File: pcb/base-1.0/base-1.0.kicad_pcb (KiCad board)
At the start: 2 copper layers, 85.6 x 54 mm, 0 parts

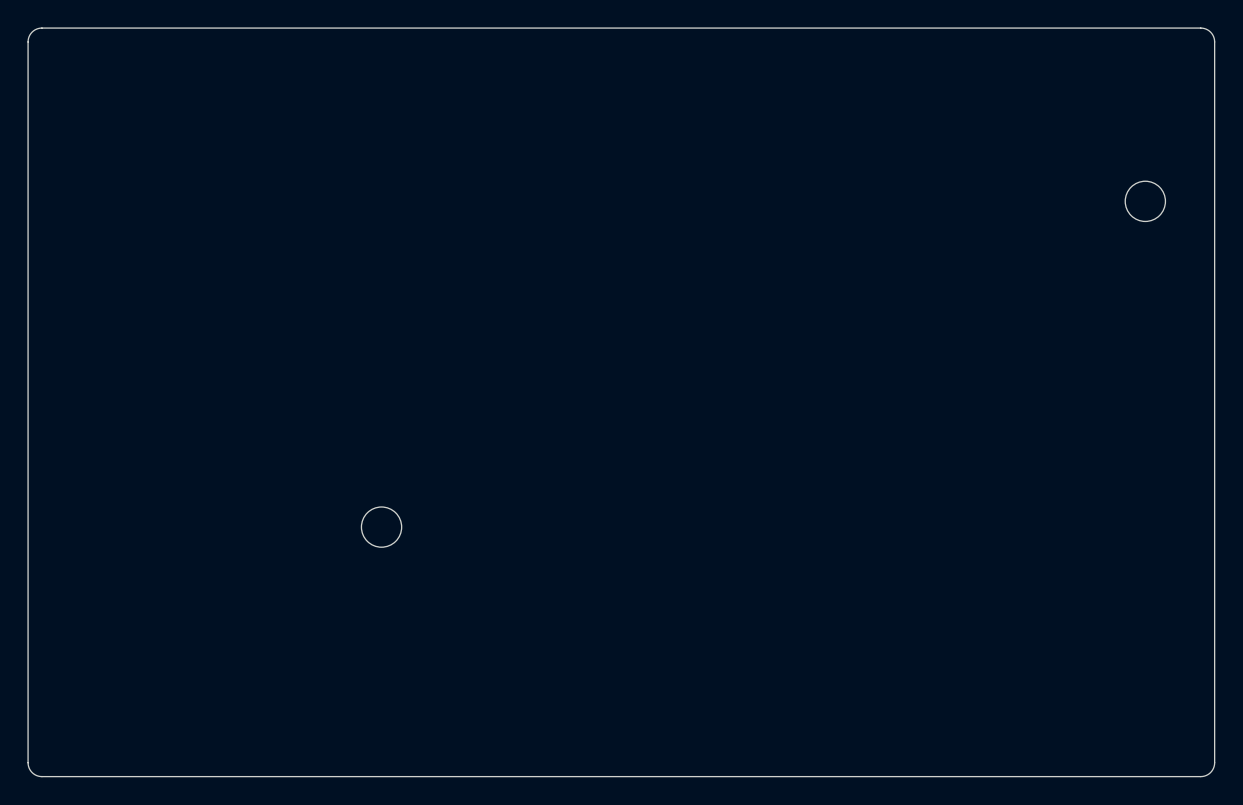
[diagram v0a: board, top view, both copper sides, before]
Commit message: o Adding IO extender for RPI header. o Adding mounting holes in schematic and PCB. o Fixing bad footprint: Capacitor_SMD:CP_Elec_8x10.2 => Capacitor_SMD:CP_Elec_8x10.
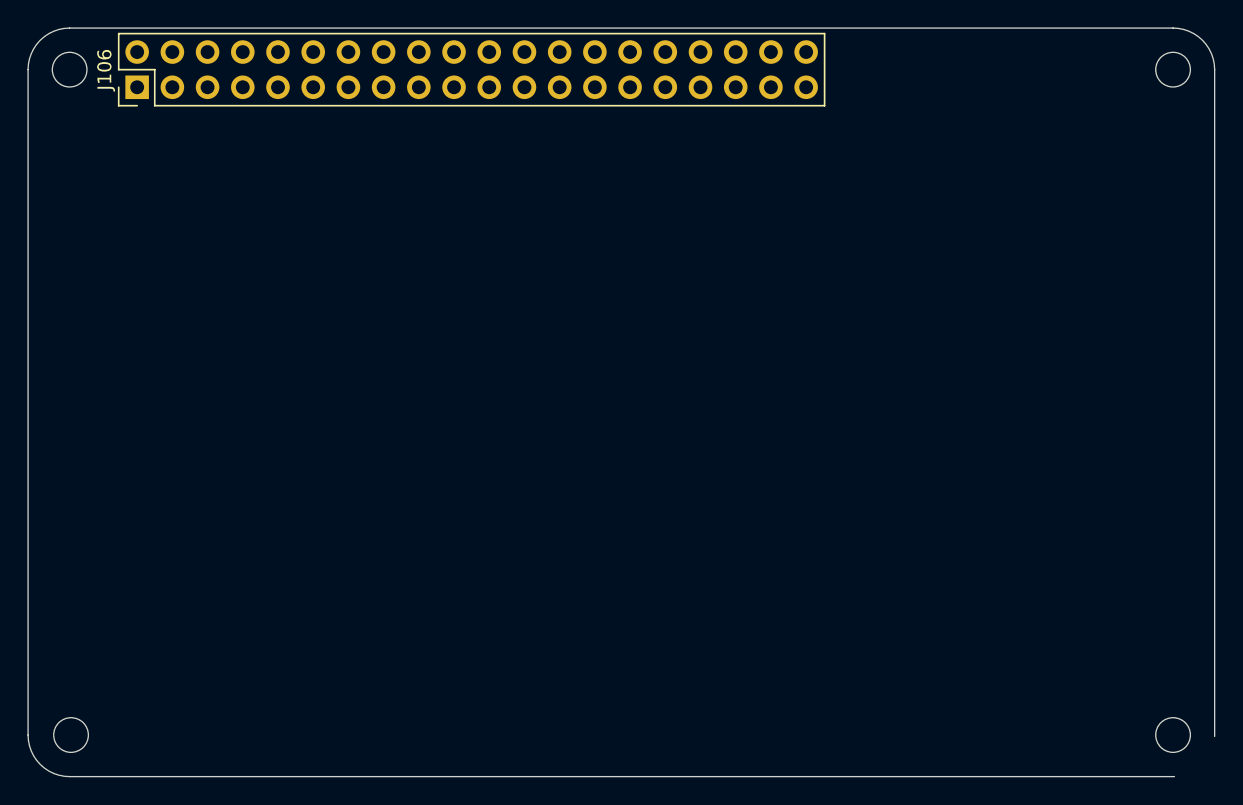
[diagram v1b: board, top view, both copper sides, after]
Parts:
- added H101: MountingHole, MountingHole:MountingHole_2.5mm, F.Cu at (111.2, 79.9)
- added H102: MountingHole, MountingHole:MountingHole_2.5mm, F.Cu at (111.3, 127.9)
- added H103: MountingHole, MountingHole:MountingHole_2.5mm, F.Cu at (190.8, 79.9)
- added H104: MountingHole, MountingHole:MountingHole_2.5mm, F.Cu at (190.8, 127.9)
- added J106: RPI_HEADER, Connector_PinHeader_2.54mm:PinHeader_2x20_P2.54mm_Vertical, F.Cu at (116.1, 81.2)
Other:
- outline, holes or cut-outs redrawn

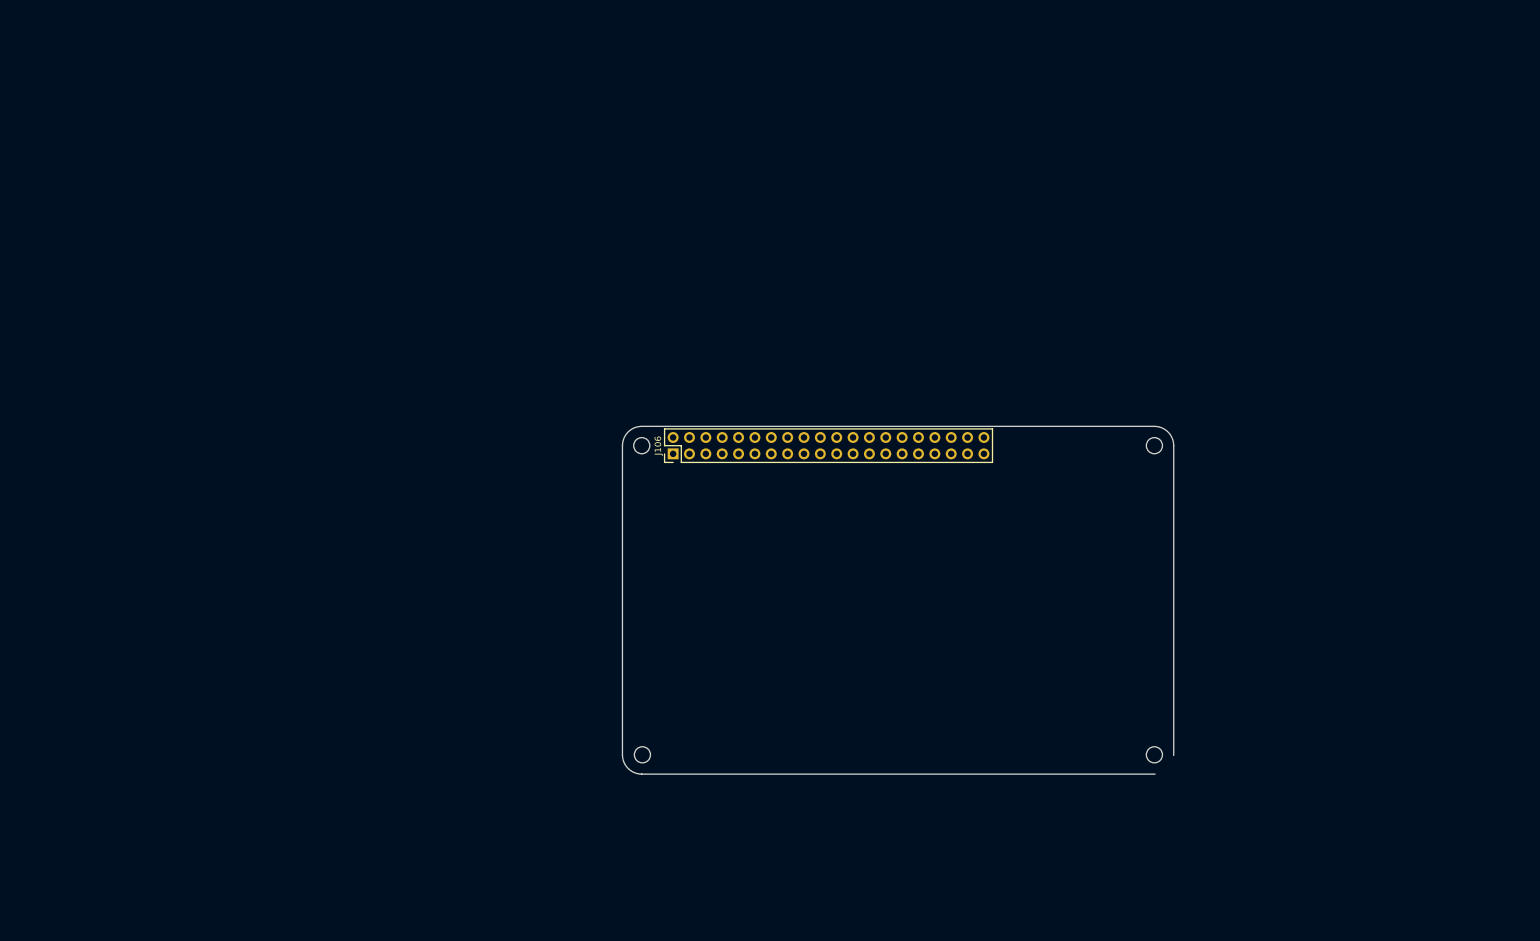
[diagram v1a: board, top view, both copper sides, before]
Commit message: o Starting on PCB. o Fixing minor issues in the schmatic while doing layout.
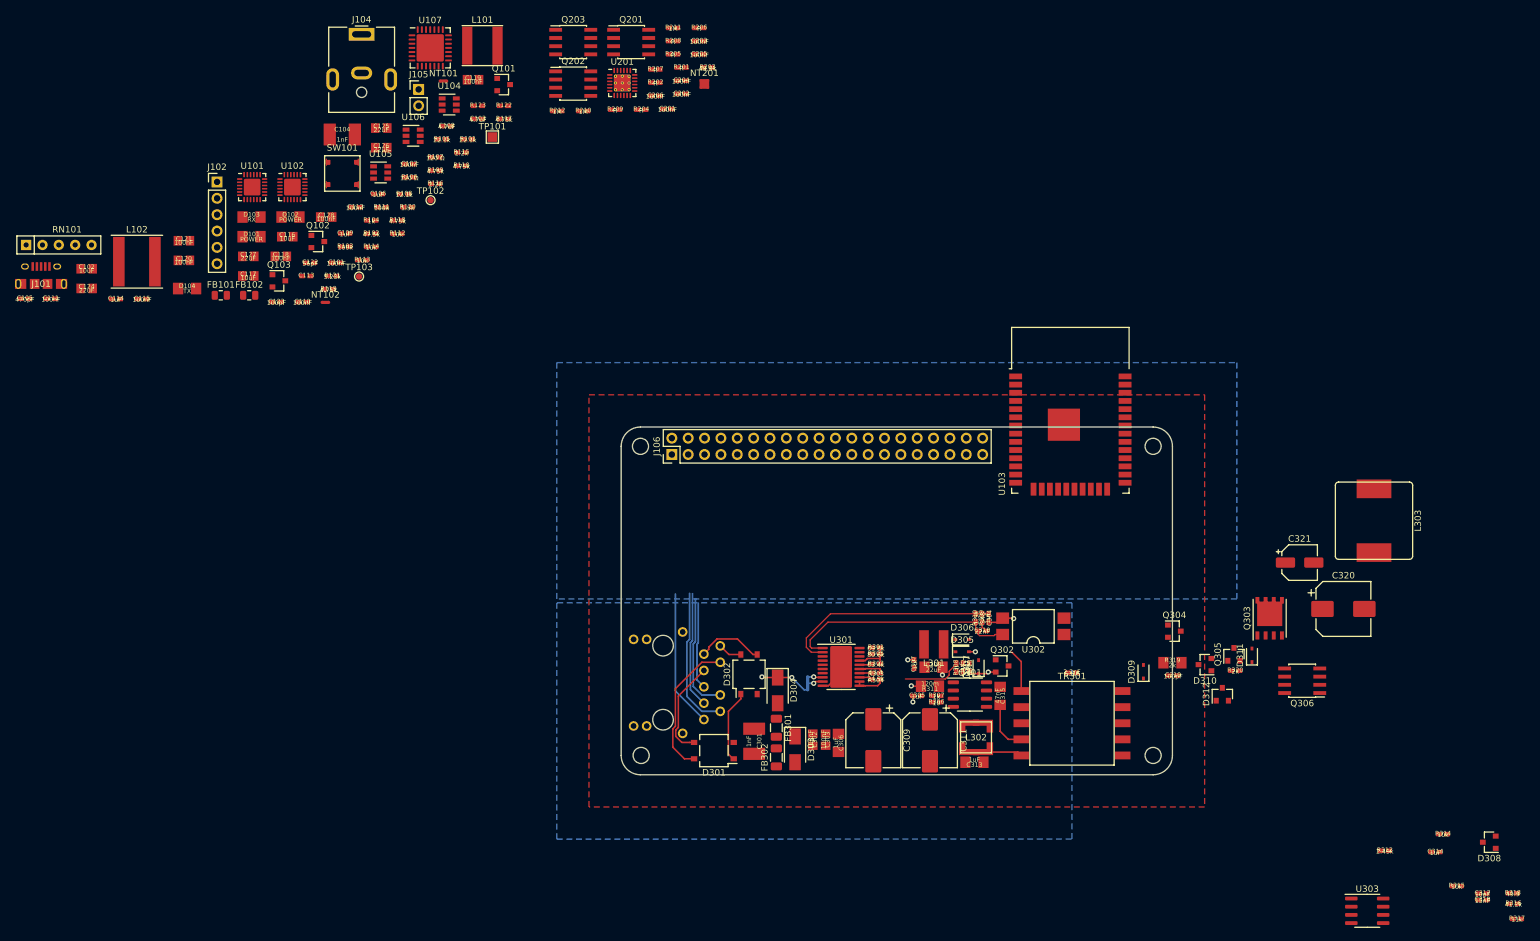
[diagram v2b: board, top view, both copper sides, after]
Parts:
- added C101: 100nF, IPC-7351-CAPC:CAPC_1005x015, F.Cu at (63.8, 51.5)
- added C102: 10uF, IPC-7351-CAPC:CAPC_2012x040, F.Cu at (25.0, 52.4)
- added C103: 4.7uF, IPC-7351-CAPC:CAPC_1005x015, F.Cu at (85.8, 29.2)
- added C104: 1nF, IPC-7351-CAPC:CAPC_4532x040, F.Cu at (64.7, 31.6)
- added C105: 470pF, IPC-7351-CAPC:CAPC_1005x015, F.Cu at (15.4, 57.1)
- added C106: 1uF, IPC-7351-CAPC:CAPC_1005x015, F.Cu at (70.2, 40.8)
- added C107: 100nF, IPC-7351-CAPC:CAPC_1005x015, F.Cu at (75.1, 36.2)
- added C108: 4.7uF, IPC-7351-CAPC:CAPC_1005x015, F.Cu at (80.9, 30.3)
- added C109: 1uF, IPC-7351-CAPC:CAPC_1005x015, F.Cu at (65.2, 47.0)
- added C110: 100nF, IPC-7351-CAPC:CAPC_1005x015, F.Cu at (58.5, 57.6)
- added C111: 100nF, IPC-7351-CAPC:CAPC_1005x015, F.Cu at (19.4, 57.1)
- added C112: 100nF, IPC-7351-CAPC:CAPC_1005x015, F.Cu at (66.8, 42.9)
- added C113: ~, IPC-7351-CAPC:CAPC_1005x015, F.Cu at (59.1, 53.5)
- added C114: 1uF, IPC-7351-CAPC:CAPC_1005x015, F.Cu at (29.6, 57.1)
- added C115: 100nF, IPC-7351-CAPC:CAPC_1005x015, F.Cu at (33.6, 57.1)
- added C116: 10uF, IPC-7351-CAPC:CAPC_2012x040, F.Cu at (56.1, 47.5)
- added C117: 10uF, IPC-7351-CAPC:CAPC_2012x040, F.Cu at (50.1, 53.5)
- added C118: 100nF, IPC-7351-CAPC:CAPC_2012x040, F.Cu at (55.1, 50.5)
- added C119: 100nF, IPC-7351-CAPC:CAPC_2012x040, F.Cu at (85.0, 23.1)
- added C120: 100nF, IPC-7351-CAPC:CAPC_2012x040, F.Cu at (40.1, 51.1)
- added C121: 100nF, IPC-7351-CAPC:CAPC_2012x040, F.Cu at (40.1, 48.1)
- added C122: 56pF, IPC-7351-CAPC:CAPC_1005x015, F.Cu at (59.7, 51.5)
- added C123: 100pF, IPC-7351-CAPC:CAPC_1005x015, F.Cu at (54.5, 57.6)
- added C124: 22uF, IPC-7351-CAPC:CAPC_2012x040, F.Cu at (25.0, 55.5)
- added C125: 22uF, IPC-7351-CAPC:CAPC_2012x040, F.Cu at (70.8, 30.6)
- added C126: 22uF, IPC-7351-CAPC:CAPC_2012x040, F.Cu at (70.8, 33.6)
- added C127: 22uF, IPC-7351-CAPC:CAPC_2012x040, F.Cu at (50.1, 50.5)
- added C128: 100nF, IPC-7351-CAPC:CAPC_2012x040, F.Cu at (62.2, 44.4)
- added C201: 100nF, IPC-7351-CAPC:CAPC_1005x015, F.Cu at (115.2, 27.6)
- added C202: 100nF, IPC-7351-CAPC:CAPC_1005x015, F.Cu at (117.4, 25.3)
- added C203: 100nF, IPC-7351-CAPC:CAPC_1005x015, F.Cu at (120.1, 17.1)
- added C204: 100nF, IPC-7351-CAPC:CAPC_1005x015, F.Cu at (117.4, 23.2)
- added C205: 100nF, IPC-7351-CAPC:CAPC_1005x015, F.Cu at (120.1, 19.1)
- added C206: 100nF, IPC-7351-CAPC:CAPC_1005x015, F.Cu at (113.3, 25.6)
- added C301: 1nF, IPC-7351-CAPC:CAPC_4532x040, F.Cu at (128.7, 125.8)
- added C302: 100nF, IPC-7351-CAPC:CAPC_2012x040, F.Cu at (137.8, 125.5)
- added C303: 100nF, IPC-7351-CAPC:CAPC_2012x040, F.Cu at (139.8, 125.5)
- added C304: 1uF, IPC-7351-CAPC:CAPC_1005x015, F.Cu at (165.1, 106.7)
- added C305: 1uF, IPC-7351-CAPC:CAPC_1005x015, F.Cu at (153.9, 118.8)
- added C306: 1uF, IPC-7351-CAPC:CAPC_3216x040, F.Cu at (141.8, 126.0)
- added C307: 1uF, IPC-7351-CAPC:CAPC_1005x015, F.Cu at (153.5, 113.8)
- added C308: 22uF, IPC-7351-CAPC:CAPC_3216x040, F.Cu at (156.5, 114.3)
- added C309: 22uF, Capacitor_SMD:CP_Elec_8x10, F.Cu at (147.2, 125.7)
- added C310: 22nF, IPC-7351-CAPC:CAPC_1005x015, F.Cu at (164.1, 108.7)
- added C311: 22uF, Capacitor_SMD:CP_Elec_8x10, F.Cu at (155.9, 125.7)
- added C312: 1uF, IPC-7351-CAPC:CAPC_1005x015, F.Cu at (161.1, 114.3)
- added C313: 1uF, IPC-7351-CAPC:CAPC_3216x040, F.Cu at (162.8, 129.1)
- added C314: 1uF, IPC-7351-CAPC:CAPC_1005x015, F.Cu at (234.4, 143.0)
- added C315: 47nF, IPC-7351-CAPC:CAPC_3216x040, F.Cu at (166.8, 118.8)
- added C316: 2.2nF, IPC-7351-CAPC:CAPC_1005x015, F.Cu at (178.0, 115.2)
- added C317: 10pF, IPC-7351-CAPC:CAPC_1005x015, F.Cu at (241.8, 149.4)
- added C318: 15nF, IPC-7351-CAPC:CAPC_1005x015, F.Cu at (241.8, 150.4)
- added C319: 100pF, IPC-7351-CAPC:CAPC_1005x015, F.Cu at (193.7, 115.6)
- added C320: 100uF, Capacitor_SMD:CP_Elec_8x10, F.Cu at (220.2, 105.2)
- added C321: 22uF, Capacitor_SMD:CP_Elec_5x5.4, F.Cu at (213.3, 98.0)
- added D101: POWER, IPC-7351-LEDSC:LEDSC_3216x060, F.Cu at (50.6, 47.5)
- added D102: POWER, IPC-7351-LEDSC:LEDSC_3216x060, F.Cu at (56.6, 44.4)
- added D103: RX, IPC-7351-LEDSC:LEDSC_3216x060, F.Cu at (50.6, 44.4)
- added D104: TX, IPC-7351-LEDSC:LEDSC_3216x060, F.Cu at (40.6, 55.5)
- added D301: CDBHD1100L-G, Package_TO_SOT_SMD:TO-269AA, F.Cu at (122.4, 127.2)
- added D302: CDBHD1100L-G, Package_TO_SOT_SMD:TO-269AA, F.Cu at (127.8, 115.4)
- added D303: SMAJ58A, Diode_SMD:D_SMA, F.Cu at (135.0, 127.0)
- added D304: SMAJ58A, Diode_SMD:D_SMA, F.Cu at (132.3, 117.9)
- added D305: BAS16, Diode_SMD:D_SOD-323, F.Cu at (160.9, 111.9)
- added D306: BAS16, Diode_SMD:D_SOD-323, F.Cu at (160.9, 110.0)
- added D307: BAS16, Diode_SMD:D_SOD-323, F.Cu at (163.5, 114.2)
- added D308: BAV99, Package_TO_SOT_SMD:SOT-23, F.Cu at (242.8, 141.5)
- added D309: BAS16, Diode_SMD:D_SOD-323, F.Cu at (189.1, 115.0)
- added D310: 12V, Diode_SMD:D_SOT-23_ANK, F.Cu at (198.7, 113.9)
- added D311: BAS16, Diode_SMD:D_SOD-323, F.Cu at (205.9, 112.5)
- added D312: 12V, Diode_SMD:D_SOT-23_ANK, F.Cu at (201.3, 118.5)
- added FB101: FBMJ2125HS250NT, Inductor_SMD:L_0805_2012Metric, F.Cu at (45.8, 56.5)
- added FB102: FBMJ2125HS250NT, Inductor_SMD:L_0805_2012Metric, F.Cu at (50.2, 56.5)
- added FB301: 500, Inductor_SMD:L_1206_3216Metric, F.Cu at (132.1, 123.7)
- added FB302: 500, Inductor_SMD:L_1206_3216Metric, F.Cu at (132.1, 128.3)
- added J101: USB_B_Micro, 10118194:10118194, F.Cu at (17.9, 54.8)
- added J102: UART, Connector_PinHeader_2.54mm:PinHeader_1x06_P2.54mm_Vertical, F.Cu at (45.2, 39.0)
- added J103: 74984104400, 74984104400:74984104400, F.Cu at (114.5, 116.7)
- added J104: Jack-DC, Connector_BarrelJack:BarrelJack_CUI_PJ-063AH_Horizontal, F.Cu at (67.7, 16.0)
- added J105: USB_GPIO, Connector_PinHeader_2.54mm:PinHeader_1x02_P2.54mm_Vertical, F.Cu at (76.5, 24.6)
- added L101: 10uH, Inductor_SMD:L_Taiyo-Yuden_NR-60xx, F.Cu at (86.5, 17.8)
- added L102: 22uH, Inductor_SMD:L_Taiyo-Yuden_NR-80xx, F.Cu at (32.8, 51.3)
- added L301: 1mH, 74404043102A:74404043102A, F.Cu at (156.6, 110.8)
- added L302: 3.3uH, 744043003:744043003, F.Cu at (163.1, 125.2)
- added L303: 22uH, 744770122:744770122, F.Cu at (224.9, 91.5)
- added NT101: Net-Tie_2, NetTie:NetTie-2_SMD_Pad0.5mm, F.Cu at (80.4, 23.3)
- added NT102: Net-Tie_2, NetTie:NetTie-2_SMD_Pad0.5mm, F.Cu at (62.1, 57.6)
- added NT201: Net-Tie_3_to_1, NetTie:NetTie-4_SMD_Pad0.5mm, F.Cu at (120.9, 23.7)
- added NT301: Net-Tie_3_Tee, NetTie:NetTie-3_SMD_Pad0.5mm, B.Cu at (136.9, 116.8)
- added Q101: BC817, Package_TO_SOT_SMD:SOT-23, F.Cu at (89.8, 23.8)
- added Q102: BC817, Package_TO_SOT_SMD:SOT-23, F.Cu at (60.9, 48.2)
- added Q103: DMP2305U-7, Package_TO_SOT_SMD:SOT-23, F.Cu at (54.9, 54.3)
- added Q201: IRF7324TRPBF, Package_SO:PowerIntegrations_SO-8, F.Cu at (109.5, 17.2)
- added Q202: IRF7324TRPBF, Package_SO:PowerIntegrations_SO-8, F.Cu at (100.5, 23.7)
- added Q203: IRF7324TRPBF, Package_SO:PowerIntegrations_SO-8, F.Cu at (100.5, 17.2)
- added Q301: Si4848DY, Package_SO:SO-8_3.9x4.9mm_P1.27mm, F.Cu at (162.2, 118.5)
- added Q302: Si2325DS, Package_TO_SOT_SMD:SOT-23, F.Cu at (167.2, 114.1)
- added Q303: Si7852DP, Package_SO:PowerPAK_SO-8_Single, F.Cu at (208.7, 106.7)
- added Q304: MMBTA06, Package_TO_SOT_SMD:SOT-23, F.Cu at (193.9, 108.7)
- added Q305: MMBTA06, Package_TO_SOT_SMD:SOT-23, F.Cu at (203.2, 112.3)
- added Q306: Si4850EY, Package_SO:PowerIntegrations_SO-8, F.Cu at (213.8, 116.4)
- added R101: 22.1k, IPC-7351-RESC:RESC_1005x015, F.Cu at (84.2, 32.3)
- added R102: 47.5k, IPC-7351-RESC:RESC_1005x015, F.Cu at (69.2, 47.0)
- added R103: 100k, IPC-7351-RESC:RESC_1005x015, F.Cu at (65.2, 49.0)
- added R104: 1k, IPC-7351-RESC:RESC_1005x015, F.Cu at (69.2, 44.9)
- added R105: 22.1k, IPC-7351-RESC:RESC_1005x015, F.Cu at (80.2, 32.3)
- added R106: 120 Ω, IPC-7351-RESC:RESC_1005x015, F.Cu at (75.1, 38.2)
- added R107: 120 Ω, IPC-7351-RESC:RESC_1005x015, F.Cu at (79.2, 35.1)
- added R108: 12.1k, IPC-7351-RESC:RESC_1005x015, F.Cu at (74.3, 40.8)
- added R109: 4.75k, IPC-7351-RESC:RESC_1005x015, F.Cu at (79.2, 37.2)
- added R110: 4.75k, IPC-7351-RESC:RESC_1005x015, F.Cu at (83.2, 36.4)
- added R111: 100k, IPC-7351-RESC:RESC_1005x015, F.Cu at (70.8, 42.9)
- added R112: 10k, IPC-7351-RESC:RESC_1005x015, F.Cu at (73.2, 47.0)
- added R113: 10k, IPC-7351-RESC:RESC_1005x015, F.Cu at (67.8, 51.1)
- added R114: 10k, IPC-7351-RESC:RESC_1005x015, F.Cu at (69.2, 49.0)
- added R115: 2.2k, IPC-7351-RESC:RESC_1005x015, F.Cu at (83.2, 34.4)
- added R116: 2.2k, IPC-7351-RESC:RESC_1005x015, F.Cu at (79.2, 39.2)
- added R117: 4.75k, IPC-7351-RESC:RESC_1005x015, F.Cu at (89.8, 29.2)
- added R118: 4.75k, IPC-7351-RESC:RESC_1005x015, F.Cu at (73.2, 44.9)
- added R119: 4.75k, IPC-7351-RESC:RESC_1005x015, F.Cu at (62.6, 55.6)
- added R120: 1.5k, IPC-7351-RESC:RESC_1005x015, F.Cu at (74.8, 42.9)
- added R121: 5.23k, IPC-7351-RESC:RESC_1005x015, F.Cu at (63.1, 53.5)
- added R122: ~, IPC-7351-RESC:RESC_1005x015, F.Cu at (89.8, 27.1)
- added R123: ~, IPC-7351-RESC:RESC_1005x015, F.Cu at (85.8, 27.1)
- added R201: R, IPC-7351-RESC:RESC_1005x015, F.Cu at (117.4, 21.2)
- added R202: R, IPC-7351-RESC:RESC_1005x015, F.Cu at (113.3, 23.5)
- added R203: 49,9k, IPC-7351-RESC:RESC_1005x015, F.Cu at (121.4, 21.2)
- added R204: R, IPC-7351-RESC:RESC_1005x015, F.Cu at (111.1, 27.7)
- added R205: R, IPC-7351-RESC:RESC_1005x015, F.Cu at (116.1, 19.1)
- added R206: R, IPC-7351-RESC:RESC_1005x015, F.Cu at (120.1, 15.0)
- added R207: R, IPC-7351-RESC:RESC_1005x015, F.Cu at (113.3, 21.5)
- added R208: R, IPC-7351-RESC:RESC_1005x015, F.Cu at (116.1, 17.1)
- added R209: R, IPC-7351-RESC:RESC_1005x015, F.Cu at (107.1, 27.7)
- added R210: 1M, IPC-7351-RESC:RESC_1005x015, F.Cu at (102.1, 27.9)
- added R211: 1M, IPC-7351-RESC:RESC_1005x015, F.Cu at (116.1, 15.0)
- added R212: 1M, IPC-7351-RESC:RESC_1005x015, F.Cu at (98.1, 27.9)
- added R301: 69.8k, IPC-7351-RESC:RESC_1005x015, F.Cu at (147.6, 111.2)
- added R302: 63.4k, IPC-7351-RESC:RESC_1005x015, F.Cu at (147.6, 113.8)
- added R303: 63.4, IPC-7351-RESC:RESC_1005x015, F.Cu at (147.6, 115.2)
- added R304: 24.9k, IPC-7351-RESC:RESC_1005x015, F.Cu at (147.6, 116.2)
- added R305: 80.6k, IPC-7351-RESC:RESC_1005x015, F.Cu at (147.6, 112.2)
- added R306: 10, IPC-7351-RESC:RESC_1005x015, F.Cu at (156.9, 119.8)
- added R307: 1k, IPC-7351-RESC:RESC_1005x015, F.Cu at (156.9, 118.8)
- added R308: 0, IPC-7351-RESC:RESC_1005x015, F.Cu at (160.1, 114.3)
- added R309: 348, IPC-7351-RESC:RESC_1005x015, F.Cu at (164.1, 106.7)
- added R310: 1.5k, IPC-7351-RESC:RESC_1005x015, F.Cu at (163.1, 106.7)
- added R311: 120m, IPC-7351-RESC:RESC_3216x040, F.Cu at (155.9, 117.2)
- added R312: 2.49k, IPC-7351-RESC:RESC_1005x015, F.Cu at (226.6, 142.8)
- added R313: 10k, IPC-7351-RESC:RESC_1005x015, F.Cu at (162.1, 114.3)
- added R314: 10k, IPC-7351-RESC:RESC_1005x015, F.Cu at (235.6, 140.2)
- added R315: 10k, IPC-7351-RESC:RESC_1005x015, F.Cu at (237.8, 148.3)
- added R316: 41.2k, IPC-7351-RESC:RESC_1005x015, F.Cu at (246.6, 151.0)
- added R317: 11k, IPC-7351-RESC:RESC_1005x015, F.Cu at (247.1, 153.4)
- added R318: 49.9, IPC-7351-RESC:RESC_1005x015, F.Cu at (246.4, 149.4)
- added R319: 2k, IPC-7351-RESC:RESC_3216x040, F.Cu at (193.6, 113.6)
- added R320: 2k, IPC-7351-RESC:RESC_1005x015, F.Cu at (203.3, 114.8)
- added RN101: R_Network04, Resistor_THT:R_Array_SIP5, F.Cu at (15.6, 48.7)
- added SW101: TL3315NF100Q, TL3315:TL3315, F.Cu at (64.7, 37.6)
- added TP101: PHY_VDDCR, TestPoint:TestPoint_Pad_1.5x1.5mm, F.Cu at (88.0, 32.0)
- added TP102: +3.3V, TestPoint:TestPoint_Pad_D1.0mm, F.Cu at (78.4, 41.8)
- added TP103: +12V, TestPoint:TestPoint_Pad_D1.0mm, F.Cu at (67.3, 53.6)
- added TR301: PA2649NL, PAxxxxNL:PAxxxxNL, F.Cu at (178.0, 123.0)
- added U101: CP2102N-A01-GQFN24, Package_DFN_QFN:QFN-24-1EP_4x4mm_P0.5mm_EP2.6x2.6mm, F.Cu at (50.7, 39.8)
- added U102: LAN8720A, Package_DFN_QFN:QFN-24-1EP_4x4mm_P0.5mm_EP2.6x2.6mm, F.Cu at (57.0, 39.8)
- added U103: ESP32-WROOM-32D, RF_Module:ESP32-WROOM-32, F.Cu at (177.8, 77.4)
- added U104: USBLC6-2SC6, Package_TO_SOT_SMD:SOT-23-6, F.Cu at (81.3, 26.9)
- added U105: TPS54202, Package_TO_SOT_SMD:SOT-23-6, F.Cu at (70.7, 37.5)
- added U106: TPS54202, Package_TO_SOT_SMD:SOT-23-6, F.Cu at (75.7, 31.8)
- added U107: MCP23S17, Package_DFN_QFN:QFN-28-1EP_6x6mm_P0.65mm_EP4.25x4.25mm, F.Cu at (78.3, 18.1)
- added U201: LTC4417, Package_DFN_QFN:QFN-24-1EP_4x4mm_P0.5mm_EP2.6x2.6mm_ThermalVias, F.Cu at (108.2, 23.6)
- added U301: TPS23754, Package_SO:HTSSOP-20-1EP_4.4x6.5mm_P0.65mm_EP3.4x6.5mm_Mask2.4x3.7mm, F.Cu at (142.2, 114.2)
- added U302: FOD817AS, Package_DIP:SMDIP-4_W9.53mm, F.Cu at (172.0, 108.0)
- added U303: TL431D, Package_SO:SOIC-8_3.9x4.9mm_P1.27mm, F.Cu at (223.8, 152.1)
- moved H103 0.22 mm to (190.6, 80.0)
- moved H104 0.22 mm to (190.6, 128.0)
- moved H101 0.22 mm to (111.0, 80.0)
- moved H102 0.22 mm to (111.1, 128.0)
- moved J106 0.22 mm to (115.9, 81.3)
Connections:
- net /MCU_IO15 renamed Net-(J106-Pad38)
- net /MCU_IO16 renamed Net-(J106-Pad35)
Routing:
- net /PoE/CTL: track 0.00 -> 35.9 mm
- net /PoE/VB: track 0.00 -> 34.2 mm
- net /ETH_TD-: track 0.00 -> 22.3 mm
- net GND_ETH: track 0.00 -> 22.1 mm, vias 0 -> 9
- net /PoE/Vin_A2: track 0.00 -> 22.0 mm
- net /ETH_TD+: track 0.00 -> 21.3 mm
- net /ETH_RD+: track 0.00 -> 18.5 mm
- net Net-(C104-Pad1): track 0.00 -> 18.0 mm
- net /PoE/Vin_A1: track 0.00 -> 15.3 mm
- net /ETH_RD-: track 0.00 -> 13.5 mm
- net Net-(C301-Pad1): track 0.00 -> 11.2 mm
- net /PoE/Vin_B1: track 0.00 -> 10.4 mm
- net /PoE/GAT2: track 0.00 -> 9.34 mm
- net /PoE/ARTN: track 0.00 -> 8.07 mm, vias 0 -> 1
- net Net-(C315-Pad2): track 0.00 -> 7.89 mm
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- added copper zone on F.Cu, net +3V3
- added copper zone on B.Cu, net GND
- added copper zone on B.Cu, net GND_ETH
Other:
- outline, holes or cut-outs redrawn
- net class Default: clearance 0.2 -> 0.15; trace_width 0.25 -> 0.15
- rule trace_clearance: 0.2 -> 0.15
- rule trace_min: 0.2 -> 0.1
